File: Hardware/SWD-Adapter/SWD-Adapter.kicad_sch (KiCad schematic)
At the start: 7 parts, among them J1 Conn_02x10_Odd_Even, J2 SWD, U1 NCP163

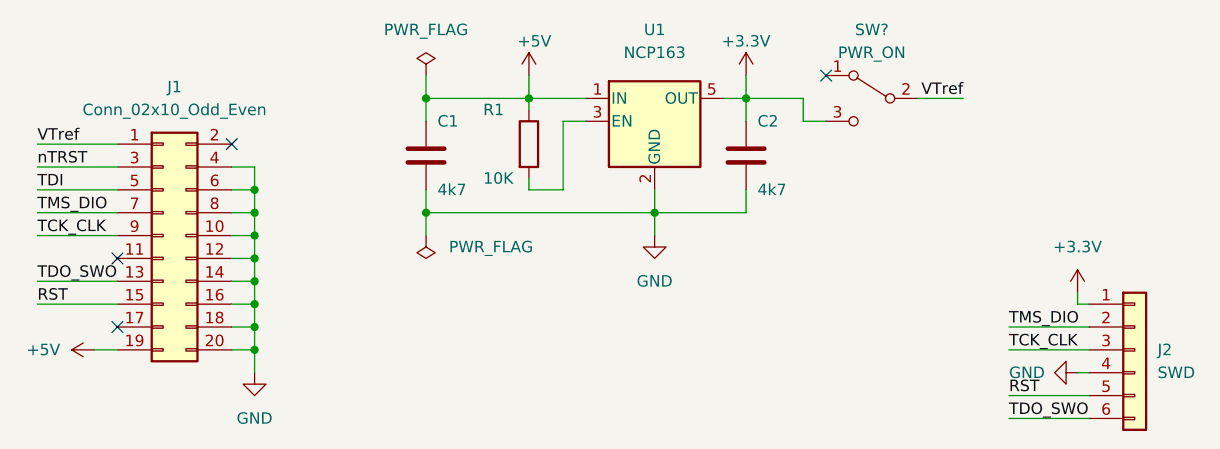
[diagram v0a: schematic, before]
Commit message: SWD Adapter for ARM
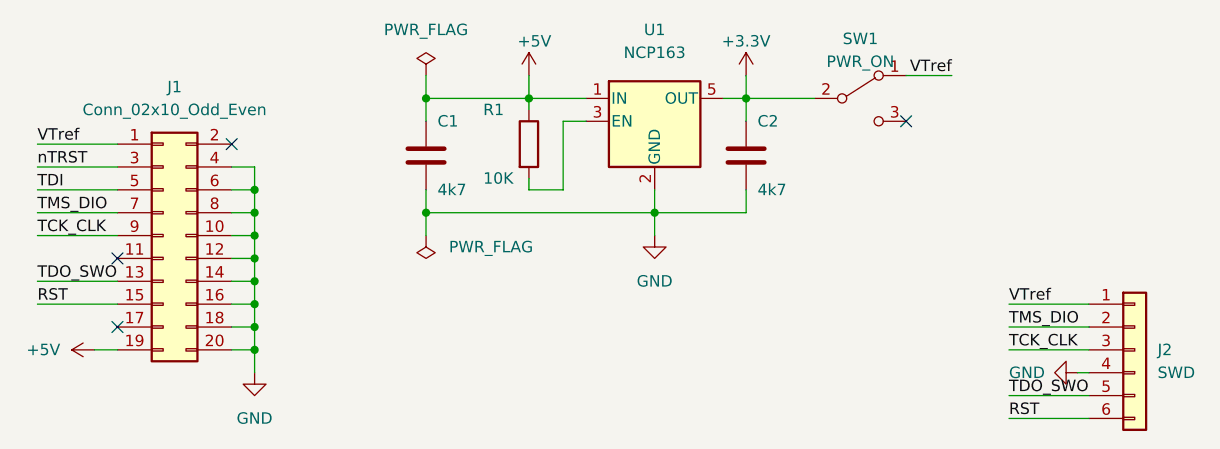
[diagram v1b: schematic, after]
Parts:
- SW1: renamed from SW?; footprint (none) -> Button_Switch_SMD:SW_SPDT_PCM12
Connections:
- net +3.3V: now also SW1.2 (B); no longer J2.1 (Pin_1), SW1.3 (C)
- net RST: now also J2.6 (Pin_6); no longer J2.5 (Pin_5)
- net TDO_SWO: now also J2.5 (Pin_5); no longer J2.6 (Pin_6)
- net VTref: now also J2.1 (Pin_1), SW1.1 (A); no longer SW1.2 (B)
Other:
- moved on the sheet: SW1
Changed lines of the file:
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@@
   (no_connect (at 68.58 86.36))
   (no_connect (at 68.58 78.74))
-  (no_connect (at 147.32 58.42))
+  (no_connect (at 156.21 63.5))
   (wire (pts (xy 128.27 73.66) (xy 128.27 76.2))
     (stroke (width 0) (type default) (color 0 0 0 0))
@@
     (stroke (width 0) (type default) (color 0 0 0 0))
   )
-  (wire (pts (xy 175.26 83.82) (xy 175.26 82.55))
-    (stroke (width 0) (type default) (color 0 0 0 0))
-  )
   (wire (pts (xy 114.3 69.85) (xy 114.3 71.12))
     (stroke (width 0) (type default) (color 0 0 0 0))
@@
     (stroke (width 0) (type default) (color 0 0 0 0))
   )
-  (wire (pts (xy 147.32 63.5) (xy 144.78 63.5))
-    (stroke (width 0) (type default) (color 0 0 0 0))
-  )
   (wire (pts (xy 59.69 76.2) (xy 68.58 76.2))
     (stroke (width 0) (type default) (color 0 0 0 0))
@@
     (stroke (width 0) (type default) (color 0 0 0 0))
   )
-  (wire (pts (xy 176.53 83.82) (xy 175.26 83.82))
+  (wire (pts (xy 167.64 83.82) (xy 176.53 83.82))
     (stroke (width 0) (type default) (color 0 0 0 0))
   )
@@
     (stroke (width 0) (type default) (color 0 0 0 0))
   )
-  (wire (pts (xy 144.78 63.5) (xy 144.78 60.96))
-    (stroke (width 0) (type default) (color 0 0 0 0))
-  )
   (wire (pts (xy 83.82 86.36) (xy 83.82 83.82))
     (stroke (width 0) (type default) (color 0 0 0 0))
   )
-  (wire (pts (xy 157.48 60.96) (xy 162.56 60.96))
+  (wire (pts (xy 156.21 58.42) (xy 161.29 58.42))
     (stroke (width 0) (type default) (color 0 0 0 0))
   )
@@
     (stroke (width 0) (type default) (color 0 0 0 0))
   )
-  (wire (pts (xy 144.78 60.96) (xy 138.43 60.96))
+  (wire (pts (xy 138.43 60.96) (xy 146.05 60.96))
     (stroke (width 0) (type default) (color 0 0 0 0))
   )
@@
     (effects (font (size 1.27 1.27)) (justify left bottom))
   )
-  (label "VTref" (at 162.56 60.96 180)
+  (label "VTref" (at 161.29 58.42 180)
     (effects (font (size 1.27 1.27)) (justify right bottom))
   )
@@
     (effects (font (size 1.27 1.27)) (justify left bottom))
   )
-  (label "TDO_SWO" (at 167.64 96.52 0)
-    (effects (font (size 1.27 1.27)) (justify left bottom))
-  )
-  (label "RST" (at 167.64 93.98 0)
+  (label "TDO_SWO" (at 167.64 93.98 0)
+    (effects (font (size 1.27 1.27)) (justify left bottom))
+  )
+  (label "RST" (at 167.64 96.52 0)
+    (effects (font (size 1.27 1.27)) (justify left bottom))
+  )
+  (label "VTref" (at 167.64 83.82 0)
     (effects (font (size 1.27 1.27)) (justify left bottom))
   )
@@
   (symbol (lib_id "power:PWR_FLAG") (at 102.87 76.2 180) (unit 1)
     (in_bom yes) (on_board yes) (fields_autoplaced)
-    (property "Reference" "#FLG0102" (id 0) (at 102.87 78.105 0)
+    (property "Reference" "#FLG02" (id 0) (at 102.87 78.105 0)
       (effects (font (size 1.27 1.27)) hide)
     )
@@
     (pin "2")
   )
-  (symbol (lib_id "power:+3.3V") (at 175.26 82.55 0) (unit 1)
-    (in_bom yes) (on_board yes) (fields_autoplaced)
-    (property "Reference" "#PWR06" (id 0) (at 175.26 86.36 0)
-      (effects (font (size 1.27 1.27)) hide)
-    )
-    (property "Value" "+3.3V" (id 1) (at 175.26 77.47 0))
-    (property "Footprint" "" (id 2) (at 175.26 82.55 0)
-      (effects (font (size 1.27 1.27)) hide)
-    )
-    (property "Datasheet" "" (id 3) (at 175.26 82.55 0)
-      (effects (font (size 1.27 1.27)) hide)
-    )
-    (pin "1")
-  )
-  (symbol (lib_id "Switch:SW_SPDT") (at 152.4 60.96 0) (mirror y) (unit 1)
-    (in_bom yes) (on_board yes) (fields_autoplaced)
-    (property "Reference" "SW?" (id 0) (at 152.4 53.34 0))
-    (property "Value" "PWR_ON" (id 1) (at 152.4 55.88 0))
-    (property "Footprint" "" (id 2) (at 152.4 60.96 0)
-      (effects (font (size 1.27 1.27)) hide)
-    )
-    (property "Datasheet" "~" (id 3) (at 152.4 60.96 0)
+  (symbol (lib_id "Switch:SW_SPDT") (at 151.13 60.96 0) (unit 1)
+    (in_bom yes) (on_board yes) (fields_autoplaced)
+    (property "Reference" "SW1" (id 0) (at 151.13 54.3392 0))
+    (property "Value" "PWR_ON" (id 1) (at 151.13 56.8761 0))
+    (property "Footprint" "Button_Switch_SMD:SW_SPDT_PCM12" (id 2) (at 151.13 60.96 0)
+      (effects (font (size 1.27 1.27)) hide)
+    )
+    (property "Datasheet" "~" (id 3) (at 151.13 60.96 0)
       (effects (font (size 1.27 1.27)) hide)
     )
@@
   (symbol (lib_id "power:PWR_FLAG") (at 102.87 58.42 0) (unit 1)
     (in_bom yes) (on_board yes) (fields_autoplaced)
-    (property "Reference" "#FLG0101" (id 0) (at 102.87 56.515 0)
+    (property "Reference" "#FLG01" (id 0) (at 102.87 56.515 0)
       (effects (font (size 1.27 1.27)) hide)
     )
@@
   (symbol_instances
     (path "/b0a806ae-7624-4ec5-9595-1863e2e35b62"
-      (reference "#FLG0101") (unit 1) (value "PWR_FLAG") (footprint "")
+      (reference "#FLG01") (unit 1) (value "PWR_FLAG") (footprint "")
     )
     (path "/0b1331ce-0f34-4c0e-aab8-d38afab7cfb2"
-      (reference "#FLG0102") (unit 1) (value "PWR_FLAG") (footprint "")
+      (reference "#FLG02") (unit 1) (value "PWR_FLAG") (footprint "")
     )
     (path "/495725cb-ecae-40d5-9992-28086fa85203"
@@
       (reference "#PWR05") (unit 1) (value "+3.3V") (footprint "")
     )
-    (path "/15cbd5c3-17ff-4d91-8107-21cc1aa2c458"
-      (reference "#PWR06") (unit 1) (value "+3.3V") (footprint "")
-    )
     (path "/c0a02d66-141a-4cd0-b08e-2c3a8c6c291e"
       (reference "#PWR07") (unit 1) (value "GND") (footprint "")
@@
     )
     (path "/1b770267-f50f-48eb-b853-1fa42b697381"
-      (reference "SW?") (unit 1) (value "PWR_ON") (footprint "")
+      (reference "SW1") (unit 1) (value "PWR_ON") (footprint "Button_Switch_SMD:SW_SPDT_PCM12")
     )
     (path "/5adb7272-955c-44d1-a639-34c6271c2d9e"
